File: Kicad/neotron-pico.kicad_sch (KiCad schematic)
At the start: 15 parts

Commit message: Swap video buffer to DIO2663
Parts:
- LOGO102: footprint Symbol:KiCad-Logo2_12mm_SilkScreen -> Symbol:KiCad-Logo2_8mm_SilkScreen
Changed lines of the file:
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@@
     )
     (property "Value" "Kicad Logo" (id 1) (at 142.875 175.895 0))
-    (property "Footprint" "Symbol:KiCad-Logo2_12mm_SilkScreen" (id 2) (at 142.875 176.0474 0)
+    (property "Footprint" "Symbol:KiCad-Logo2_8mm_SilkScreen" (id 2) (at 142.875 176.0474 0)
       (effects (font (size 1.27 1.27)) hide)
     )
@@
     )
     (path "/00000000-0000-0000-0000-00005fe412eb"
-      (reference "LOGO102") (unit 1) (value "Kicad Logo") (footprint "Symbol:KiCad-Logo2_12mm_SilkScreen")
+      (reference "LOGO102") (unit 1) (value "Kicad Logo") (footprint "Symbol:KiCad-Logo2_8mm_SilkScreen")
     )
     (path "/00000000-0000-0000-0000-00005fe3e77b"
@@
     )
     (path "/00000000-0000-0000-0000-000060687f8a/00000000-0000-0000-0000-00005feaf8c1"
-      (reference "U401") (unit 1) (value "THS7316") (footprint "Package_SO:SOIC-8_3.9x4.9mm_P1.27mm")
+      (reference "U401") (unit 1) (value "DIO2663") (footprint "Package_SO:SOIC-8_3.9x4.9mm_P1.27mm")
     )
     (path "/00000000-0000-0000-0000-000060687f8a/00000000-0000-0000-0000-00005fea7855"

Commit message: Updated to KiCAD 7.
Had to move a net-tie to resolve a "too close" error.
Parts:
- LOGO101, LOGO102, LOGO103: now left out of the parts list

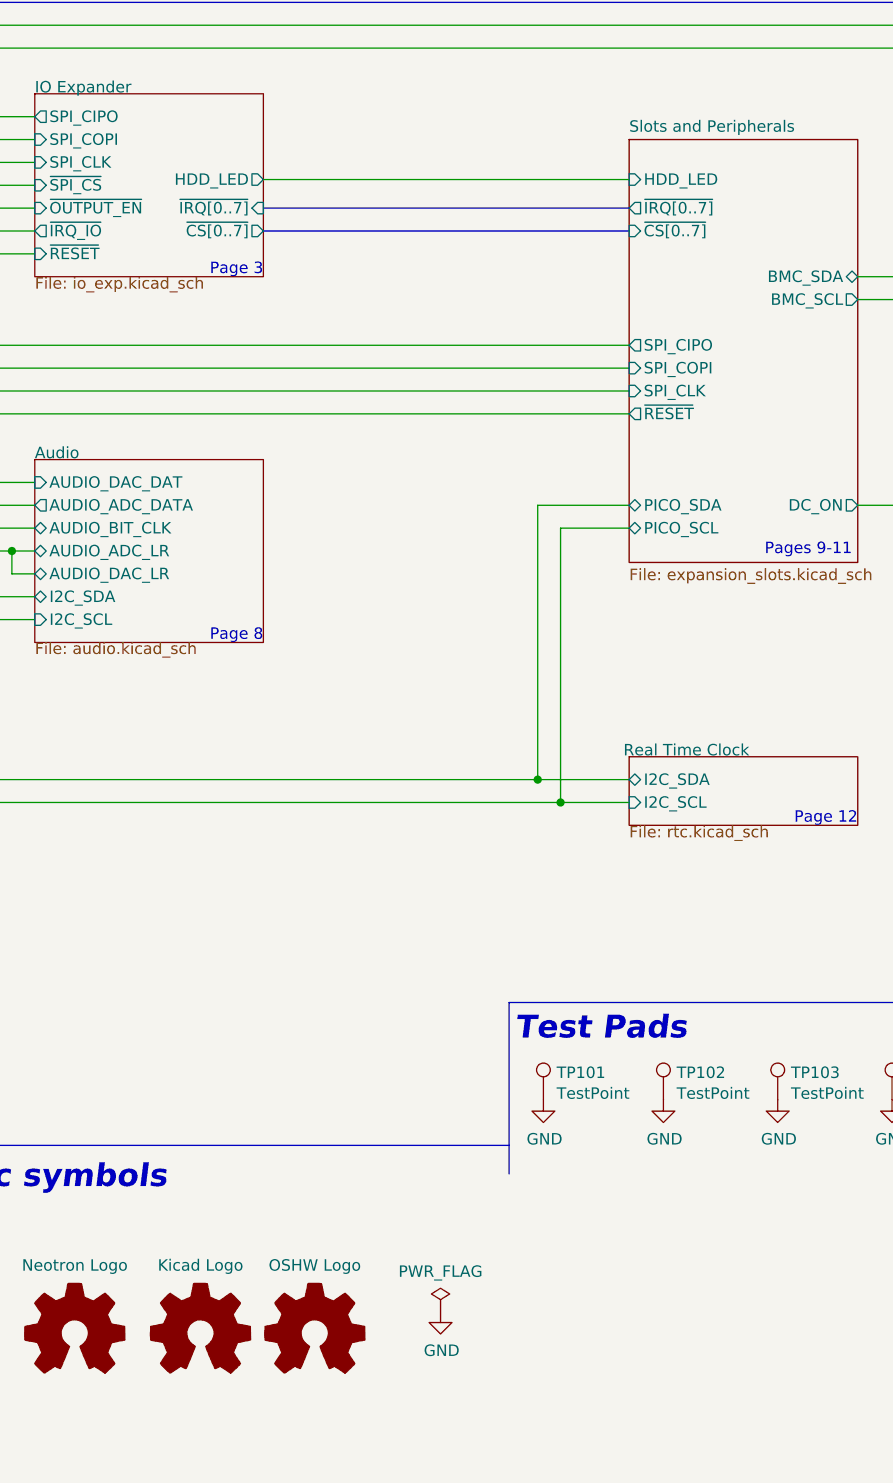
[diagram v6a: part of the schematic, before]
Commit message: Updated to Kicad 8.0.3.
Had to disable PCB/Library footprint mismatch, and schematic grid alignment errors (I was on 25mil, Kicad really wants to use 50mil).
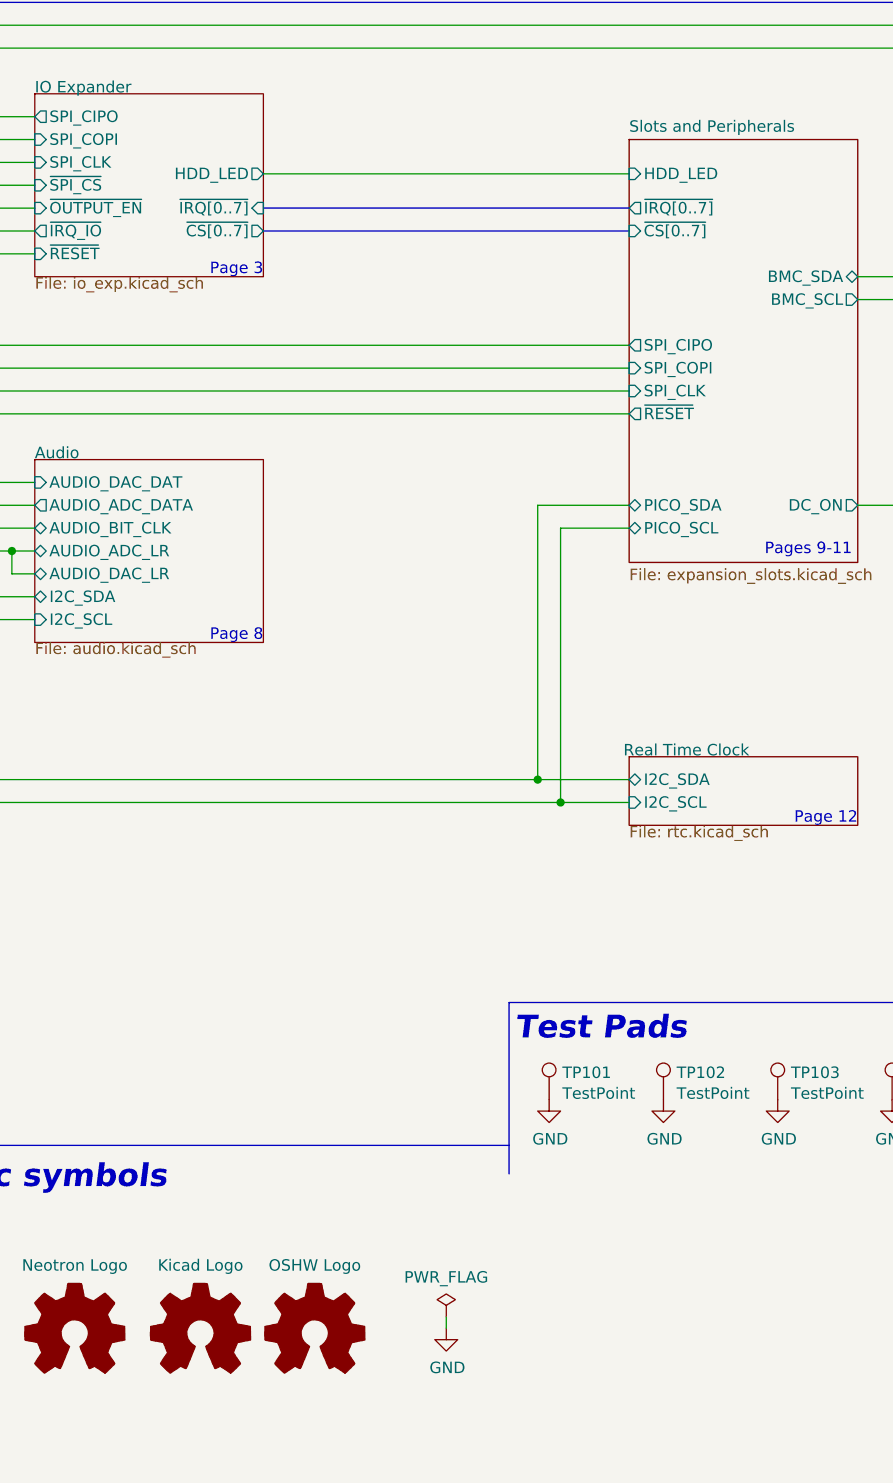
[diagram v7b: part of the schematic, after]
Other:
- moved on the sheet: TP101
